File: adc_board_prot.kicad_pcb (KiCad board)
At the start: 6 copper layers, 146 x 148 mm, 389 parts, among them J1 USB4105-GF-A, J2 TMJG4820GENL, J3 5747841-4, J4 5747841-4, SW1 SDA02H1SBDR, SW2 FSM6JSMATR, U1 ADA4945-1, U10 LT3579, U11 LT3093, U12 LT8624S, U13 LT3045, U14 LT3045, U15 LT3045, U16 LT3045, U17 ADA4945-1, U18 LTC2387-18, U19 ADA4945-1, U2 LTC2387-18, U20 LTC2387-18, U21 ADA4945-1, U22 LTC2387-18, U23 24LC16BT-I/OT, U24 Si5342A-D, U25 ADA4898-2, U26 ADA4898-2, U27 ADA4898-2, U28 ADA4898-2, U3 93AA56BT-I/OT, U4 FT2232HL, U5 TVS1800DRV, U6 TPS259480AYWPR, U7 LT8642S, U8 LT8350S, U9 LT3042, X1 ECS-2520MVLC-120-CN-TR, Y1 CX3225SB48000D0FLJCC

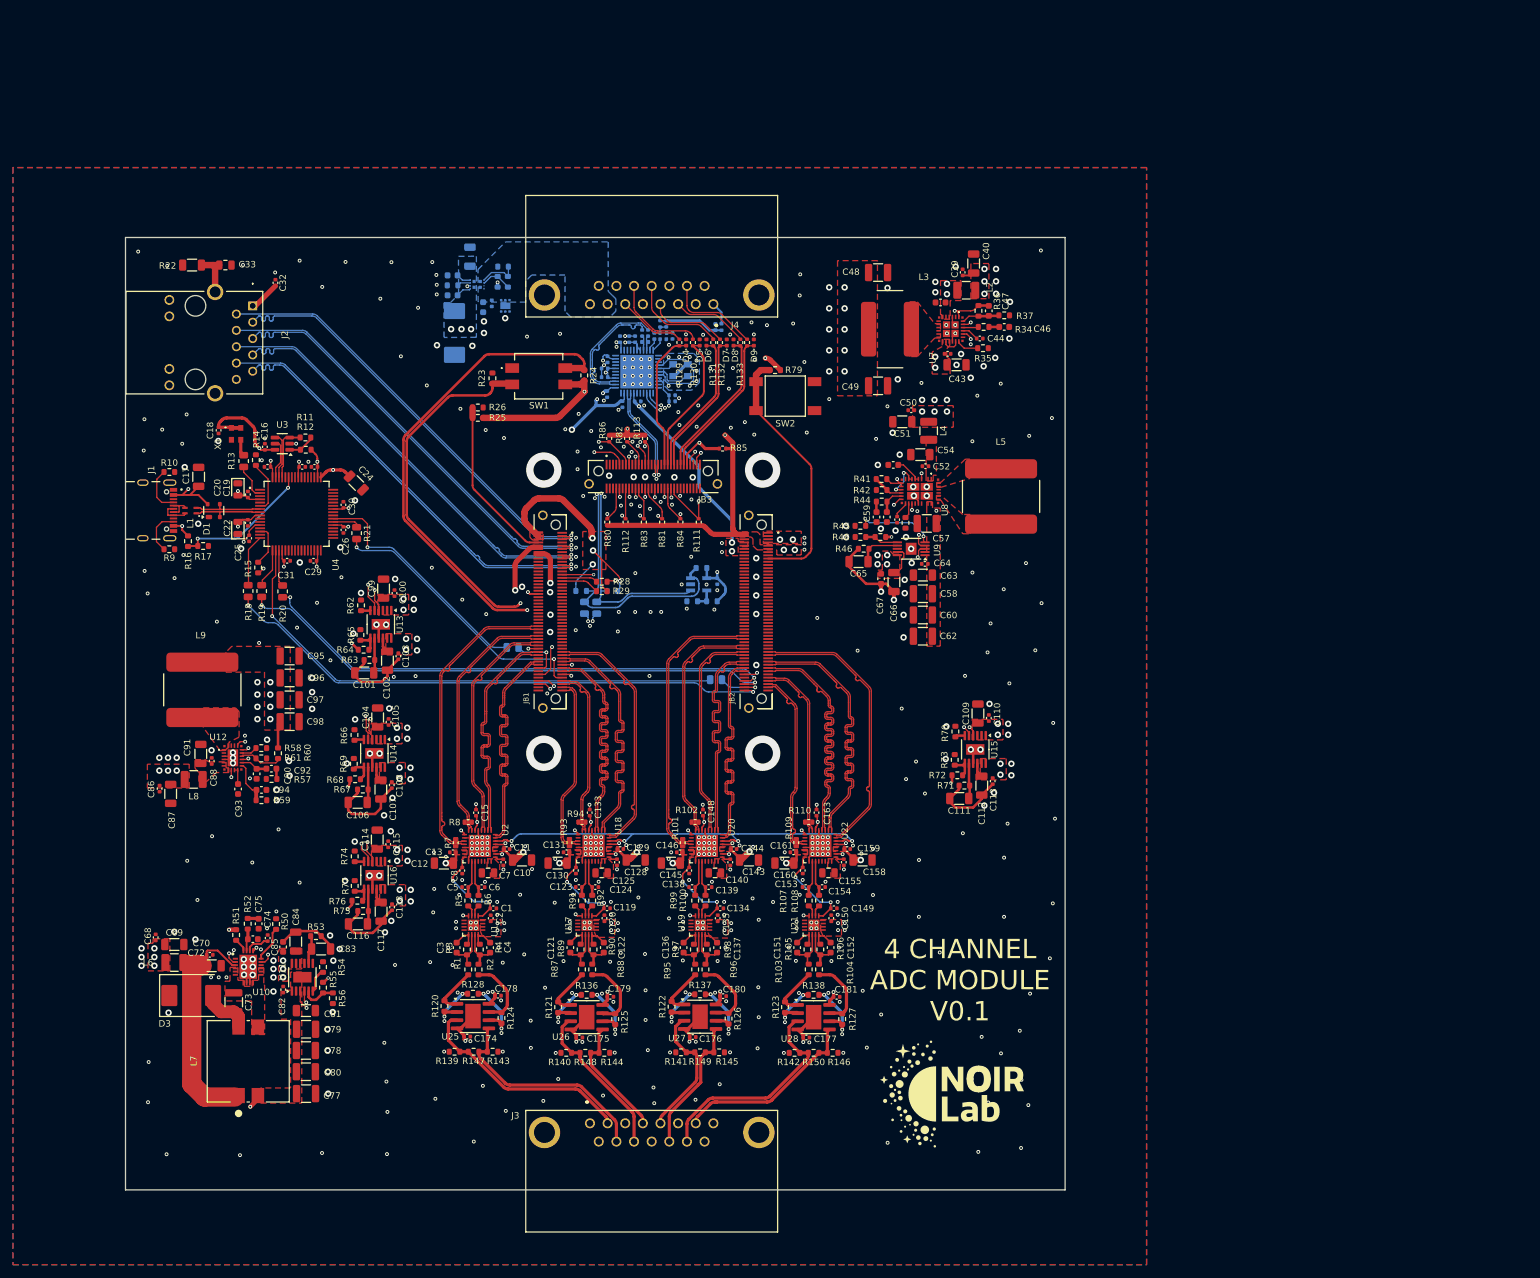
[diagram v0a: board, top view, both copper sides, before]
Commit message: Split DC DC schematic and improve layout
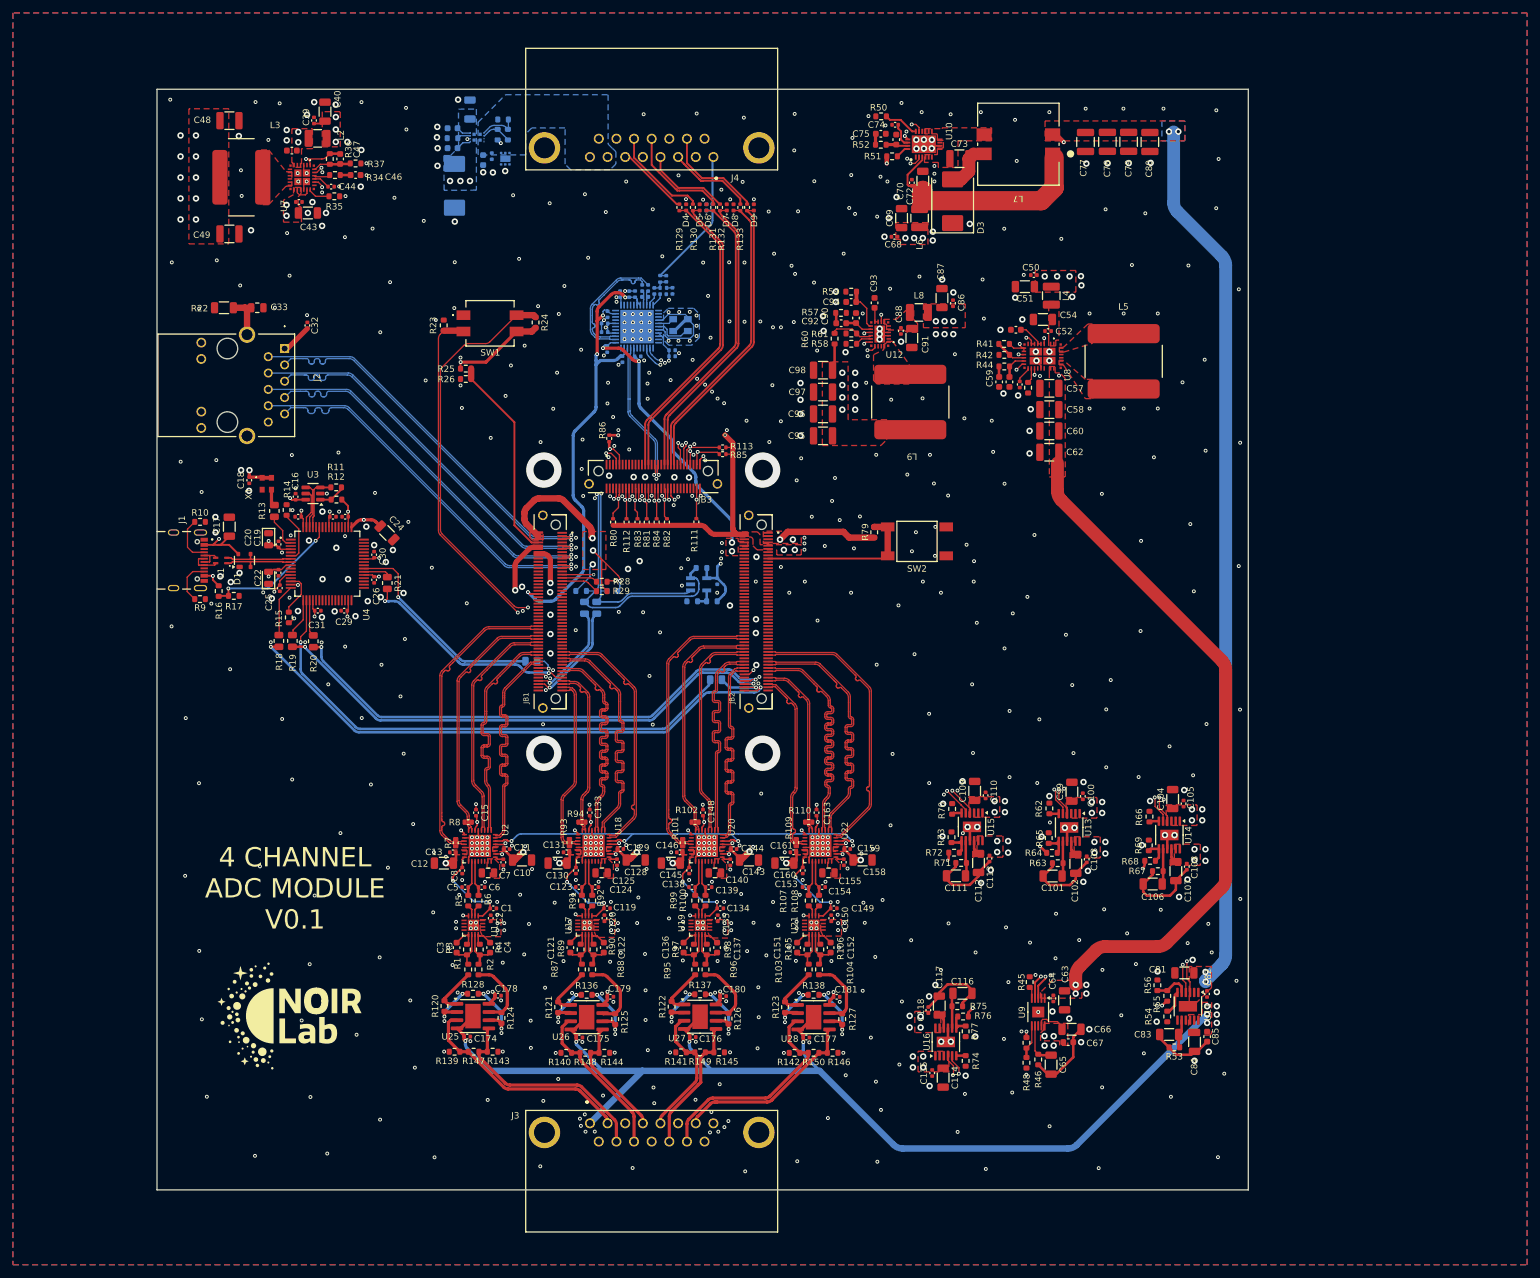
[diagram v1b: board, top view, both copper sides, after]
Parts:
- D2: value 20V -> B520C-13-F
- moved C80 195.1 mm to (229.2, -2.48), turned to -90 degrees
- moved C77 191.1 mm to (219.2, -2.48), turned to -90 degrees
- moved C78 188.3 mm to (222.6, -2.50), turned to -90 degrees
- moved C79 188.0 mm to (225.9, -2.50), turned to -90 degrees
- moved L7 186.1 mm to (208.7, -2.13), turned to 180 degrees
- moved C73 172.9 mm to (199.6, 0.12), turned to 0 degrees
- moved D3 171.0 mm to (198.5, 6.73), turned to 90 degrees
- moved U10 165.4 mm to (194.1, -2.13), turned to 90 degrees
- moved C72 164.6 mm to (193.9, 3.55), turned to 90 degrees
- moved L6 163.7 mm to (193.4, 9.35), turned to 90 degrees
- moved C70 162.2 mm to (192.2, 3.85), turned to 90 degrees
- moved C69 159.7 mm to (190.6, 9.35), turned to 90 degrees
- moved C74 159.6 mm to (189.6, -5.15), turned to 180 degrees
- moved C76 159.5 mm to (189.8, -2.85), turned to 90 degrees
- moved C68 158.2 mm to (189.5, 12.2), turned to 180 degrees
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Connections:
- net /power/+15VA/+15V5A_IN renamed /power/+15V5A/+15V5A_IN
- net /power/+15VA/+15V5A_OUT renamed +15V5A
- net /power/+15VA/+15V5A_SW1 renamed /power/+15V5A/+15V5A_SW1
- net /power/+15VA/+15V5A_SW2 renamed /power/+15V5A/+15V5A_SW2
- net /power/-15VA/-15V5A_D renamed /power/-15V5A/-15V5A_D
- net /power/-15VA/-15V5A_IN renamed /power/-15V5A/-15V5A_IN
- net /power/-15VA/-15V5A_OUT renamed -15V5A
- net /power/-15VA/-15V5A_SW renamed /power/-15V5A/-15V5A_SW
- D4 pad 1: B34_L21+ -> B34_L10+
- D5 pad 1: B34_L21- -> B34_L10-
- D6 pad 1: B34_L15+ -> B34_L21+
- D7 pad 1: B34_L15- -> B34_L21-
- D8 pad 1: B34_L17+ -> B34_L15+
- D9 pad 1: B34_L17- -> B34_L15-
- JB3 pad 10: 4V2A_EN -> 4V2A_PG
- JB3 pad 13: 5V5A_PG -> unconnected-(JB3-P20|B34|T2|L18P-Pad13)
- JB3 pad 14: -15V5A_PG -> 2V5D_PG
- JB3 pad 15: 5V5A_SYNC -> unconnected-(JB3-P21|B34|T2|L18N-Pad15)
- JB3 pad 16: -15V5A_SYNC -> 2V5D_EN
- JB3 pad 19: 2V5A_EN -> unconnected-(JB3-P17|B34|T3|L20P-Pad19)
- JB3 pad 20: -15V5A_EN -> 15VA_PG
- JB3 pad 21: 2V5A_PG -> unconnected-(JB3-P18|B34|T3|L20N-Pad21)
- JB3 pad 22: -15VA_PG -> 15VA_EN
- JB3 pad 25: 5VA_EN -> B34_L10+
- JB3 pad 26: -15VA_EN -> 5VA_PG
- JB3 pad 27: 5VA_PG -> B34_L10-
- JB3 pad 28: 2V5D_PG -> 5VA_EN
- JB3 pad 32: 2V5D_EN -> -15VA_PG
- JB3 pad 34: unconnected-(JB3-L19|B34|T1|MRCC|L12N-Pad34) -> -15VA_EN
- JB3 pad 38: 15VA_EN -> 2V5A_PG
- JB3 pad 40: 15VA_PG -> 2V5A_EN
- JB3 pad 44: 15V5A_PG -> unconnected-(JB3-K21|B34|Y1|DQS|L9N-Pad44)
- JB3 pad 47: B34_L17+ -> -15V5A_EN
- JB3 pad 49: B34_L17- -> -15V5A_SYNC
- JB3 pad 51: 3V3D_PG -> -15V5A_PG
- JB3 pad 53: 3V3D_SYNC -> 5V5A_EN
- JB3 pad 57: 15V5A_EN -> 5V5A_PG
- JB3 pad 58: unconnected-(JB3-R19|B34|T3|L22P-Pad58) -> 15V5A_PG
- JB3 pad 59: unconnected-(JB3-N20|B34|SRCC|L14N-Pad59) -> 5V5A_SYNC
- JB3 pad 60: unconnected-(JB3-T19|B34|T3|L22N-Pad60) -> 15V5A_EN
- JB3 pad 7: unconnected-(JB3-J15|B34|T0|L1P-Pad7) -> 3V3D_SYNC
- JB3 pad 8: 4V2A_PG -> 4V2A_EN
- JB3 pad 9: 5V5A_EN -> 3V3D_PG
- R112 pad 1: -15V5A_PG -> 2V5D_PG
- R113 pad 1: 5VA_PG -> -15V5A_PG
- R129 pad 1: B34_L21+ -> B34_L10+
- R130 pad 1: B34_L21- -> B34_L10-
- R131 pad 1: B34_L15+ -> B34_L21+
- R132 pad 1: B34_L15- -> B34_L21-
- R133 pad 1: B34_L17+ -> B34_L15+
- R134 pad 1: B34_L17- -> B34_L15-
- R81 pad 1: 2V5D_PG -> 5VA_PG
- R83 pad 1: -15VA_PG -> 15VA_PG
- R84 pad 1: 15VA_PG -> -15VA_PG
- R85 pad 1: 3V3D_PG -> 5V5A_PG
- R86 pad 1: 5V5A_PG -> 3V3D_PG
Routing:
- net -15V5A: track 40.4 -> 176.3 mm, vias 2 -> 6
- net 5V5A: track 81.0 -> 212.4 mm
- net 12V: track 271.1 -> 143.4 mm
- net +15V5A: track 14.9 -> 121.6 mm, vias 2 -> 4
- net 15VA_PG: track 49.3 -> 130.8 mm
- net 15VA_EN: track 47.0 -> 127.9 mm
- net +15VA: track 243.7 -> 173.4 mm
- net 5V5A_SYNC: track 105.2 -> 37.2 mm
- net 5V5A_EN: track 107.6 -> 41.6 mm
- net 5V5A_PG: track 104.6 -> 39.8 mm
- net -15V5A_EN: track 131.7 -> 70.0 mm
- net -15V5A_PG: track 125.7 -> 67.2 mm
- net 4V2A_PG: track 80.1 -> 137.0 mm
- net 4V2A_EN: track 77.9 -> 134.0 mm
- net -15V5A_SYNC: track 118.5 -> 65.7 mm
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- added copper zone on In2.Cu, net +15V5A
- added copper zone on In2.Cu, net +15VA
- added copper zone on B.Cu, net -15V5A
- added copper zone on In2.Cu, net -15V5A
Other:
- board size 146 x 148 mm -> 169.6 x 171 mm
